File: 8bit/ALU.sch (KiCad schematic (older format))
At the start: 0 parts

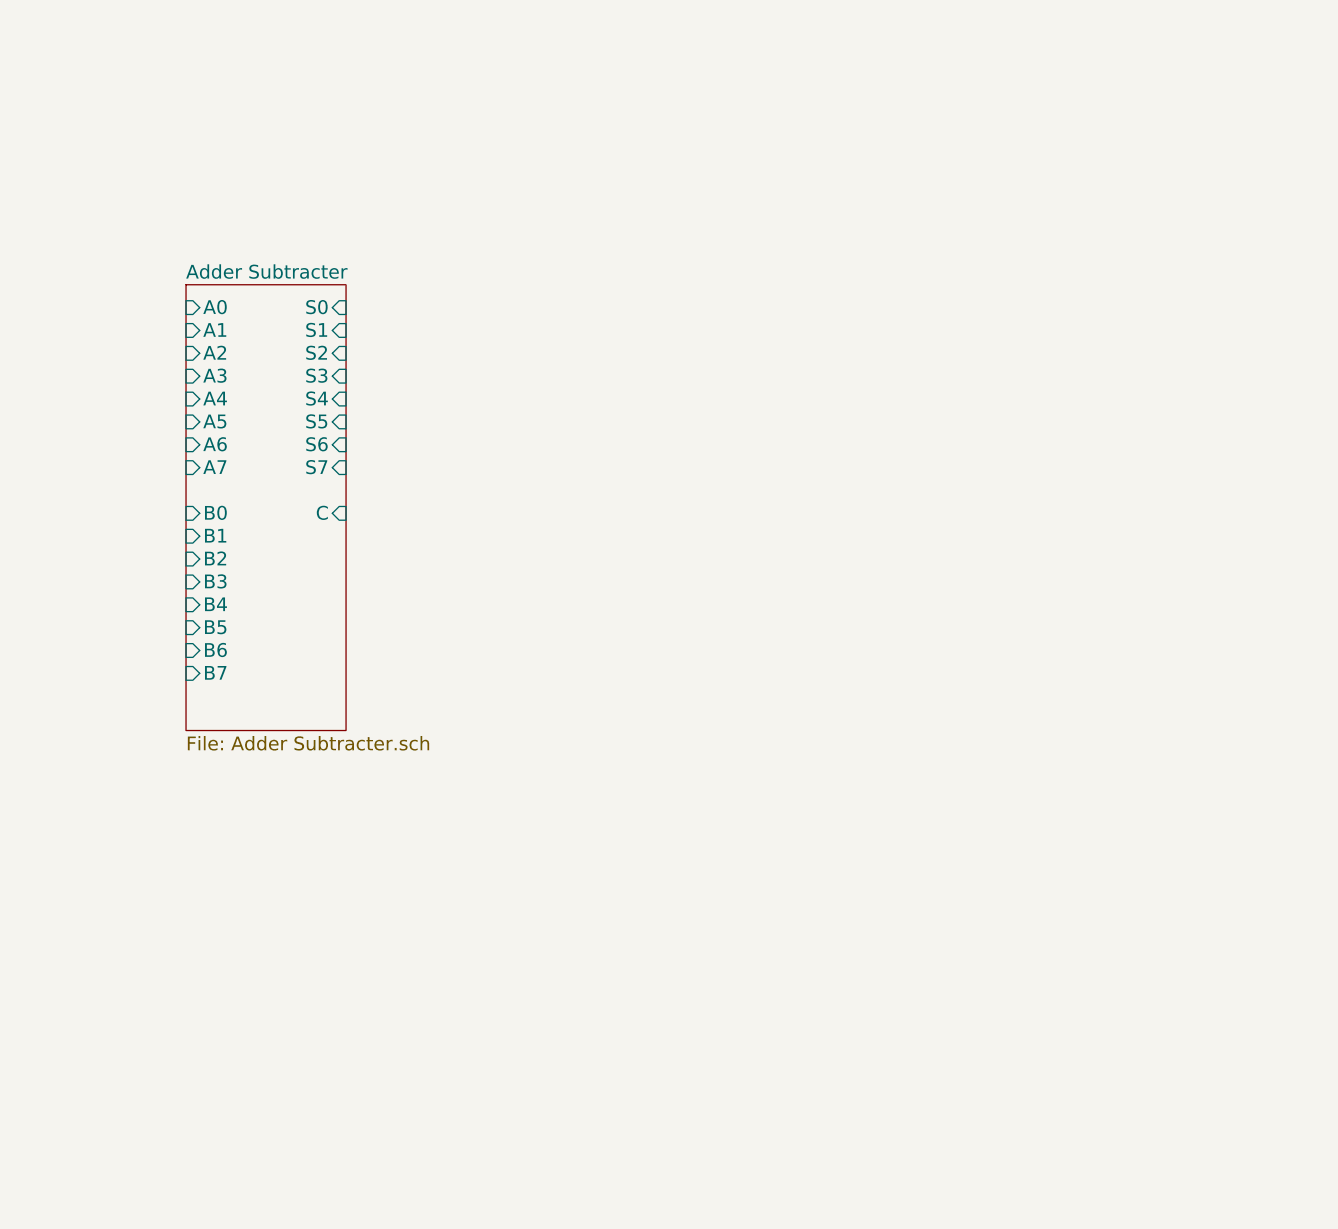
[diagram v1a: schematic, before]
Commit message: Created 16:8 mux sheet for simplicity
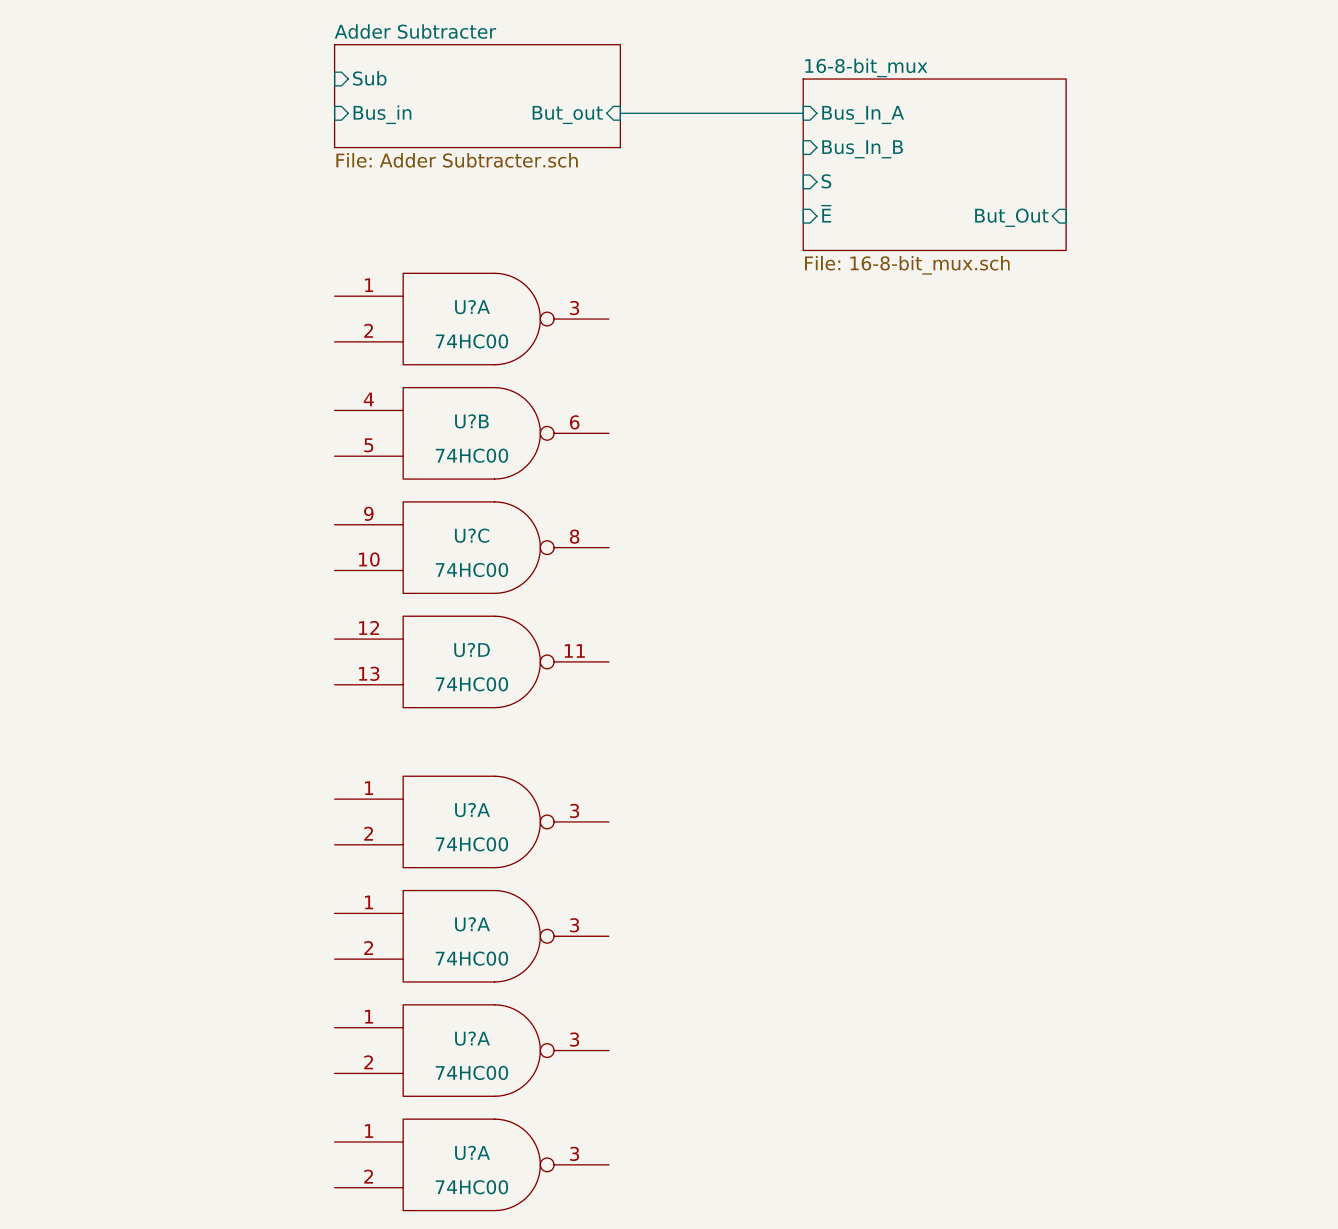
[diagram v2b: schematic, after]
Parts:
- added U? (x8): 74HC00, symbol 74HC00
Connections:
- new net GND: U?.7 (GND), U?.7 (GND), U?.7 (GND), U?.7 (GND), U?.7 (GND), U?.7 (GND), U?.7 (GND), U?.7 (GND)
- new net VCC: U?.14 (VCC), U?.14 (VCC), U?.14 (VCC), U?.14 (VCC), U?.14 (VCC), U?.14 (VCC), U?.14 (VCC), U?.14 (VCC)
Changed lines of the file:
@@
 $Descr A4 11693 8268
 encoding utf-8
-Sheet 2 27
+Sheet 2 28
 Title ""
 Date ""
@@
 $EndDescr
 $Sheet
-S 3100 3000 700  1950
+S 3750 1950 1250 450
 U 5495DFEE
 F0 "Adder Subtracter" 60
 F1 "Adder Subtracter.sch" 60
-F2 "A1" I L 3100 3200 60
-F3 "A2" I L 3100 3300 60
-F4 "B2" I L 3100 4200 60
-F5 "A3" I L 3100 3400 60
-F6 "B3" I L 3100 4300 60
-F7 "A4" I L 3100 3500 60
-F8 "B4" I L 3100 4400 60
-F9 "A0" I L 3100 3100 60
-F10 "B1" I L 3100 4100 60
-F11 "A5" I L 3100 3600 60
-F12 "B5" I L 3100 4500 60
-F13 "A6" I L 3100 3700 60
-F14 "B6" I L 3100 4600 60
-F15 "A7" I L 3100 3800 60
-F16 "B7" I L 3100 4700 60
-F17 "B0" I L 3100 4000 60
-F18 "S0" I R 3800 3100 60
-F19 "S1" I R 3800 3200 60
-F20 "S2" I R 3800 3300 60
-F21 "S3" I R 3800 3400 60
-F22 "S4" I R 3800 3500 60
-F23 "S5" I R 3800 3600 60
-F24 "S6" I R 3800 3700 60
-F25 "S7" I R 3800 3800 60
-F26 "C" I R 3800 4000 60
+F2 "Bus_in" I L 3750 2250 60
+F3 "But_out" I R 5000 2250 60
+F4 "Sub" I L 3750 2100 60
 $EndSheet
+$Sheet
+S 5800 2100 1150 750
+U 549E42AB
+F0 "16-8-bit_mux" 60
+F1 "16-8-bit_mux.sch" 60
+F2 "Bus_In_A" I L 5800 2250 60
+F3 "Bus_In_B" I L 5800 2400 60
+F4 "But_Out" I R 6950 2700 60
+F5 "S" I L 5800 2550 60
+F6 "~E" I L 5800 2700 60
+$EndSheet
+Wire Bus Line
+	5000 2250 5800 2250
+$Comp
+L 74HC00 U?
+U 1 1 549E5951
+P 4350 3150
+F 0 "U?" H 4350 3200 60  0000 C CNN
+F 1 "74HC00" H 4350 3050 60  0000 C CNN
+F 2 "" H 4350 3150 60  0000 C CNN
+F 3 "" H 4350 3150 60  0000 C CNN
+	1    4350 3150
+	1    0    0    -1
+$EndComp
+$Comp
+L 74HC00 U?
+U 2 1 549E59F7
+P 4350 3650
+F 0 "U?" H 4350 3700 60  0000 C CNN
+F 1 "74HC00" H 4350 3550 60  0000 C CNN
+F 2 "" H 4350 3650 60  0000 C CNN
+F 3 "" H 4350 3650 60  0000 C CNN
+	2    4350 3650
+	1    0    0    -1
+$EndComp
+$Comp
+L 74HC00 U?
+U 3 1 549E5A9A
+P 4350 4150
+F 0 "U?" H 4350 4200 60  0000 C CNN
+F 1 "74HC00" H 4350 4050 60  0000 C CNN
+F 2 "" H 4350 4150 60  0000 C CNN
+F 3 "" H 4350 4150 60  0000 C CNN
+	3    4350 4150
+	1    0    0    -1
+$EndComp
+$Comp
+L 74HC00 U?
+U 4 1 549E5AF6
+P 4350 4650
+F 0 "U?" H 4350 4700 60  0000 C CNN
+F 1 "74HC00" H 4350 4550 60  0000 C CNN
+F 2 "" H 4350 4650 60  0000 C CNN
+F 3 "" H 4350 4650 60  0000 C CNN
+	4    4350 4650
+	1    0    0    -1
+$EndComp
+$Comp
+L 74HC00 U?
+U 1 1 549E5C32
+P 4350 5350
+F 0 "U?" H 4350 5400 60  0000 C CNN
+F 1 "74HC00" H 4350 5250 60  0000 C CNN
+F 2 "" H 4350 5350 60  0000 C CNN
+F 3 "" H 4350 5350 60  0000 C CNN
+	1    4350 5350
+	1    0    0    -1
+$EndComp
+$Comp
+L 74HC00 U?
+U 1 1 549E5C38
+P 4350 5850
+F 0 "U?" H 4350 5900 60  0000 C CNN
+F 1 "74HC00" H 4350 5750 60  0000 C CNN
+F 2 "" H 4350 5850 60  0000 C CNN
+F 3 "" H 4350 5850 60  0000 C CNN
+	1    4350 5850
+	1    0    0    -1
+$EndComp
+$Comp
+L 74HC00 U?
+U 1 1 549E5C3E
+P 4350 6350
+F 0 "U?" H 4350 6400 60  0000 C CNN
+F 1 "74HC00" H 4350 6250 60  0000 C CNN
+F 2 "" H 4350 6350 60  0000 C CNN
+F 3 "" H 4350 6350 60  0000 C CNN
+	1    4350 6350
+	1    0    0    -1
+$EndComp
+$Comp
+L 74HC00 U?
+U 1 1 549E5C44
+P 4350 6850
+F 0 "U?" H 4350 6900 60  0000 C CNN
+F 1 "74HC00" H 4350 6750 60  0000 C CNN
+F 2 "" H 4350 6850 60  0000 C CNN
+F 3 "" H 4350 6850 60  0000 C CNN
+	1    4350 6850
+	1    0    0    -1
+$EndComp
 $EndSCHEMATC

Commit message: Created 8-bit NAND Sheet, added to ALU
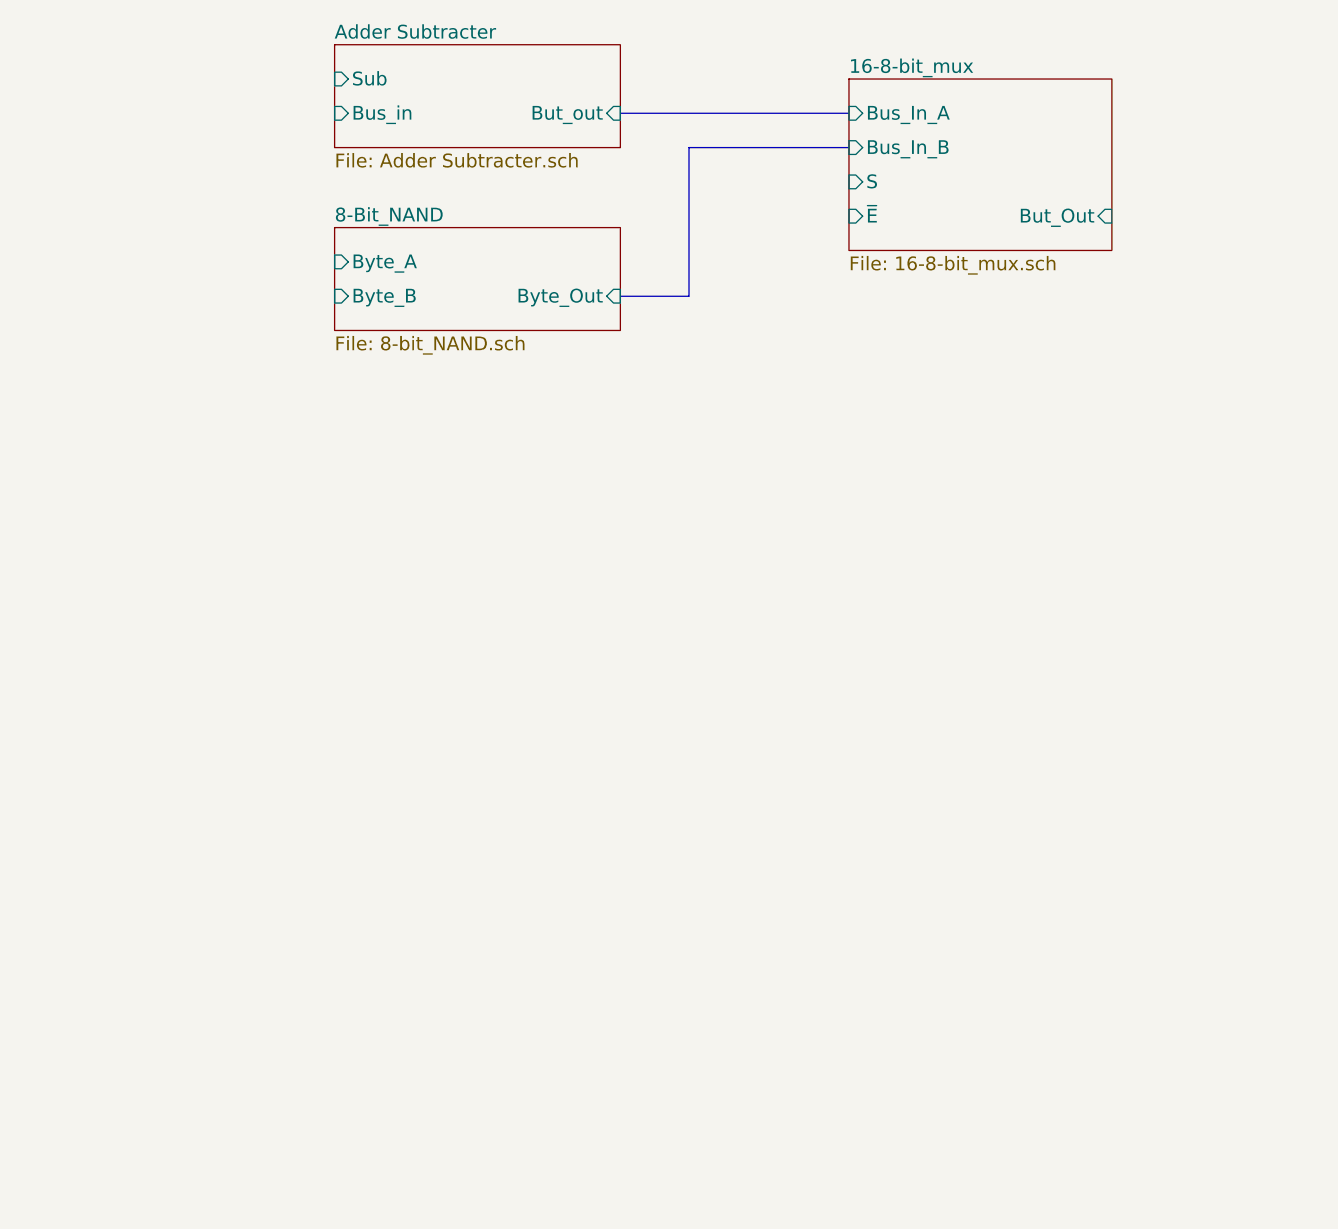
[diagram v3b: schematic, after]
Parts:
- removed U? (x8): 74HC00, symbol 74HC00
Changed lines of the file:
@@
 $Descr A4 11693 8268
 encoding utf-8
-Sheet 2 28
+Sheet 2 29
 Title ""
 Date ""
@@
 $EndSheet
 $Sheet
-S 5800 2100 1150 750
+S 6000 2100 1150 750
 U 549E42AB
 F0 "16-8-bit_mux" 60
 F1 "16-8-bit_mux.sch" 60
-F2 "Bus_In_A" I L 5800 2250 60
-F3 "Bus_In_B" I L 5800 2400 60
-F4 "But_Out" I R 6950 2700 60
-F5 "S" I L 5800 2550 60
-F6 "~E" I L 5800 2700 60
+F2 "Bus_In_A" I L 6000 2250 60
+F3 "Bus_In_B" I L 6000 2400 60
+F4 "But_Out" I R 7150 2700 60
+F5 "S" I L 6000 2550 60
+F6 "~E" I L 6000 2700 60
 $EndSheet
 Wire Bus Line
-	5000 2250 5800 2250
-$Comp
-L 74HC00 U?
-U 1 1 549E5951
-P 4350 3150
-F 0 "U?" H 4350 3200 60  0000 C CNN
-F 1 "74HC00" H 4350 3050 60  0000 C CNN
-F 2 "" H 4350 3150 60  0000 C CNN
-F 3 "" H 4350 3150 60  0000 C CNN
-	1    4350 3150
-	1    0    0    -1
-$EndComp
-$Comp
-L 74HC00 U?
-U 2 1 549E59F7
-P 4350 3650
-F 0 "U?" H 4350 3700 60  0000 C CNN
-F 1 "74HC00" H 4350 3550 60  0000 C CNN
-F 2 "" H 4350 3650 60  0000 C CNN
-F 3 "" H 4350 3650 60  0000 C CNN
-	2    4350 3650
-	1    0    0    -1
-$EndComp
-$Comp
-L 74HC00 U?
-U 3 1 549E5A9A
-P 4350 4150
-F 0 "U?" H 4350 4200 60  0000 C CNN
-F 1 "74HC00" H 4350 4050 60  0000 C CNN
-F 2 "" H 4350 4150 60  0000 C CNN
-F 3 "" H 4350 4150 60  0000 C CNN
-	3    4350 4150
-	1    0    0    -1
-$EndComp
-$Comp
-L 74HC00 U?
-U 4 1 549E5AF6
-P 4350 4650
-F 0 "U?" H 4350 4700 60  0000 C CNN
-F 1 "74HC00" H 4350 4550 60  0000 C CNN
-F 2 "" H 4350 4650 60  0000 C CNN
-F 3 "" H 4350 4650 60  0000 C CNN
-	4    4350 4650
-	1    0    0    -1
-$EndComp
-$Comp
-L 74HC00 U?
-U 1 1 549E5C32
-P 4350 5350
-F 0 "U?" H 4350 5400 60  0000 C CNN
-F 1 "74HC00" H 4350 5250 60  0000 C CNN
-F 2 "" H 4350 5350 60  0000 C CNN
-F 3 "" H 4350 5350 60  0000 C CNN
-	1    4350 5350
-	1    0    0    -1
-$EndComp
-$Comp
-L 74HC00 U?
-U 1 1 549E5C38
-P 4350 5850
-F 0 "U?" H 4350 5900 60  0000 C CNN
-F 1 "74HC00" H 4350 5750 60  0000 C CNN
-F 2 "" H 4350 5850 60  0000 C CNN
-F 3 "" H 4350 5850 60  0000 C CNN
-	1    4350 5850
-	1    0    0    -1
-$EndComp
-$Comp
-L 74HC00 U?
-U 1 1 549E5C3E
-P 4350 6350
-F 0 "U?" H 4350 6400 60  0000 C CNN
-F 1 "74HC00" H 4350 6250 60  0000 C CNN
-F 2 "" H 4350 6350 60  0000 C CNN
-F 3 "" H 4350 6350 60  0000 C CNN
-	1    4350 6350
-	1    0    0    -1
-$EndComp
-$Comp
-L 74HC00 U?
-U 1 1 549E5C44
-P 4350 6850
-F 0 "U?" H 4350 6900 60  0000 C CNN
-F 1 "74HC00" H 4350 6750 60  0000 C CNN
-F 2 "" H 4350 6850 60  0000 C CNN
-F 3 "" H 4350 6850 60  0000 C CNN
-	1    4350 6850
-	1    0    0    -1
-$EndComp
+	5000 2250 6000 2250
+Wire Bus Line
+	5300 2400 6000 2400
+$Sheet
+S 3750 2750 1250 450
+U 549E892D
+F0 "8-Bit_NAND" 60
+F1 "8-bit_NAND.sch" 60
+F2 "Byte_A" I L 3750 2900 60
+F3 "Byte_B" I L 3750 3050 60
+F4 "Byte_Out" I R 5000 3050 60
+$EndSheet
+Wire Bus Line
+	5000 3050 5300 3050
+Wire Bus Line
+	5300 3050 5300 2400
 $EndSCHEMATC

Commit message: Added Comparator to ALU, removed NAND
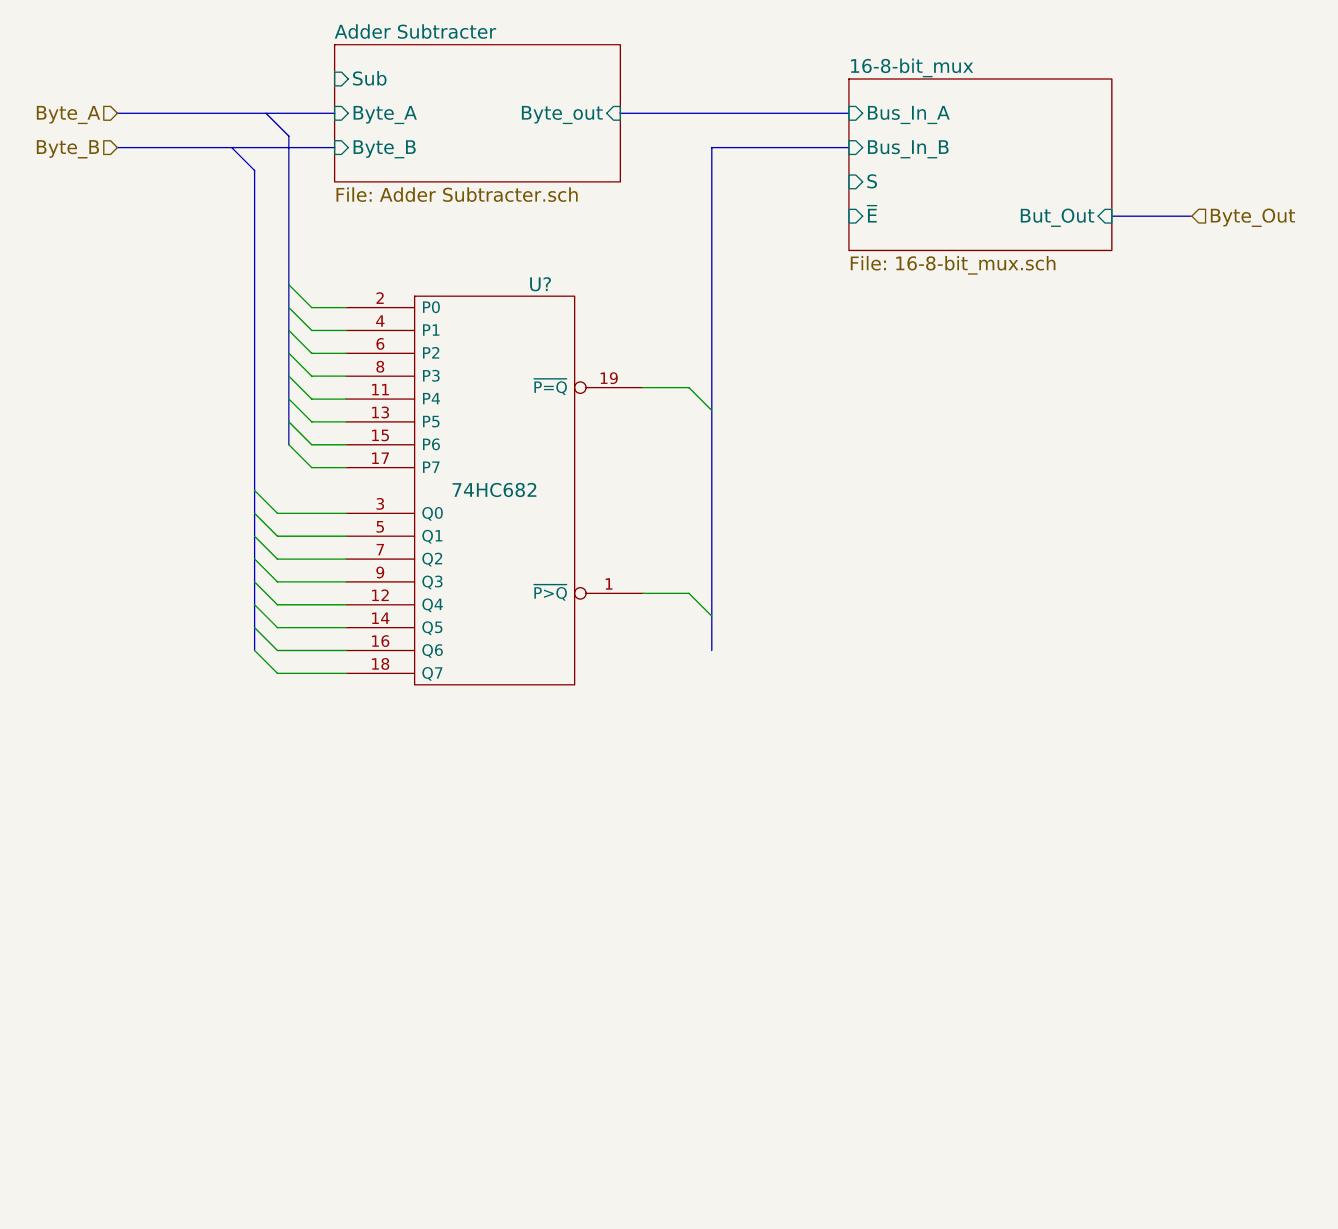
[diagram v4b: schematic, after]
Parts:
- added U?: 74HC682, symbol 74HC682
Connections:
- new net Gnd: U?.10 (Gnd)
- new net Vcc: U?.20 (Vcc)
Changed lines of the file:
@@
 $Descr A4 11693 8268
 encoding utf-8
-Sheet 2 29
+Sheet 2 28
 Title ""
 Date ""
@@
 $EndDescr
 $Sheet
-S 3750 1950 1250 450
+S 3750 1950 1250 600
 U 5495DFEE
 F0 "Adder Subtracter" 60
 F1 "Adder Subtracter.sch" 60
-F2 "Bus_in" I L 3750 2250 60
-F3 "But_out" I R 5000 2250 60
-F4 "Sub" I L 3750 2100 60
+F2 "Sub" I L 3750 2100 60
+F3 "Byte_out" I R 5000 2250 60
+F4 "Byte_A" I L 3750 2250 60
+F5 "Byte_B" I L 3750 2400 60
 $EndSheet
 $Sheet
@@
 Wire Bus Line
 	5000 2250 6000 2250
+$Comp
+L 74HC682 U?
+U 1 1 549EBB6E
+P 4450 3900
+F 0 "U?" H 4650 4800 60  0000 C CNN
+F 1 "74HC682" H 4450 3900 60  0000 C CNN
+F 2 "" H 4350 3900 60  0000 C CNN
+F 3 "" H 4350 3900 60  0000 C CNN
+	1    4450 3900
+	1    0    0    -1
+$EndComp
+Wire Wire Line
+	5100 3450 5300 3450
+Wire Wire Line
+	5100 4350 5300 4350
+Entry Wire Line
+	5300 3450 5400 3550
+Entry Wire Line
+	5300 4350 5400 4450
 Wire Bus Line
-	5300 2400 6000 2400
-$Sheet
-S 3750 2750 1250 450
-U 549E892D
-F0 "8-Bit_NAND" 60
-F1 "8-bit_NAND.sch" 60
-F2 "Byte_A" I L 3750 2900 60
-F3 "Byte_B" I L 3750 3050 60
-F4 "Byte_Out" I R 5000 3050 60
-$EndSheet
+	5400 2400 5400 4600
 Wire Bus Line
-	5000 3050 5300 3050
+	5400 2400 6000 2400
+Wire Wire Line
+	3500 4000 3800 4000
+Wire Wire Line
+	3500 4100 3800 4100
+Wire Wire Line
+	3500 4200 3800 4200
+Wire Wire Line
+	3500 4300 3800 4300
+Wire Wire Line
+	3500 4400 3800 4400
+Wire Wire Line
+	3500 4500 3800 4500
+Wire Wire Line
+	3500 4600 3800 4600
+Wire Wire Line
+	3500 4700 3800 4700
+Entry Wire Line
+	3550 3000 3650 3100
+Entry Wire Line
+	3550 3100 3650 3200
+Entry Wire Line
+	3550 3200 3650 3300
+Entry Wire Line
+	3550 3300 3650 3400
+Entry Wire Line
+	3550 3400 3650 3500
+Entry Wire Line
+	3550 3500 3650 3600
+Entry Wire Line
+	3550 3600 3650 3700
+Entry Wire Line
+	3550 3700 3650 3800
+Entry Wire Line
+	3400 3900 3500 4000
+Entry Wire Line
+	3400 4000 3500 4100
+Entry Wire Line
+	3400 4100 3500 4200
+Entry Wire Line
+	3400 4200 3500 4300
+Entry Wire Line
+	3400 4300 3500 4400
+Entry Wire Line
+	3400 4400 3500 4500
+Entry Wire Line
+	3400 4500 3500 4600
+Entry Wire Line
+	3400 4600 3500 4700
 Wire Bus Line
-	5300 3050 5300 2400
+	3550 2350 3550 3700
+Wire Bus Line
+	3400 2500 3400 4600
+Entry Bus Bus
+	3450 2250 3550 2350
+Wire Bus Line
+	2800 2250 3750 2250
+Entry Bus Bus
+	3300 2400 3400 2500
+Wire Bus Line
+	2800 2400 3750 2400
+Wire Wire Line
+	3650 3100 3800 3100
+Wire Wire Line
+	3800 3200 3650 3200
+Wire Wire Line
+	3650 3300 3800 3300
+Wire Wire Line
+	3800 3400 3650 3400
+Wire Wire Line
+	3650 3500 3800 3500
+Wire Wire Line
+	3800 3600 3650 3600
+Wire Wire Line
+	3650 3700 3800 3700
+Wire Wire Line
+	3800 3800 3650 3800
+Text HLabel 2800 2250 0    60   Input ~ 0
+Byte_A
+Text HLabel 2800 2400 0    60   Input ~ 0
+Byte_B
+Wire Bus Line
+	7150 2700 7500 2700
+Text HLabel 7500 2700 2    60   Input ~ 0
+Byte_Out
 $EndSCHEMATC
